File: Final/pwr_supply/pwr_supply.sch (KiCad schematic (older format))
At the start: 28 parts, among them IC1 AP64350SP-13, IC2 AP64350SP-13, T1 Transformer_1P_SS

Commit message: 
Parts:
- added C13, C14: 100n, Capacitor_SMD:C_1206_3216Metric_Pad1.33x1.80mm_HandSolder, symbol pspice:CAP
- C10, C9: footprint SamacSys_Parts:CAPC1608X90N -> Capacitor_SMD:C_1206_3216Metric_Pad1.33x1.80mm_HandSolder
- C11, C12: footprint SamacSys_Parts:CAPPRD225W50D680H1250 -> Capacitor_SMD:C_1206_3216Metric_Pad1.33x1.80mm_HandSolder
- C4, C8: footprint SamacSys_Parts:CAPC1005X56N -> Capacitor_SMD:C_1206_3216Metric_Pad1.33x1.80mm_HandSolder
- R5, R8: value 115k -> 309k
- RV1: footprint Varistor:RV_Disc_D15.5mm_W4.2mm_P7.5mm -> Varistor:RV_Disc_D16.5mm_W6.7mm_P7.5mm
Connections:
- wire segments 95 -> 98

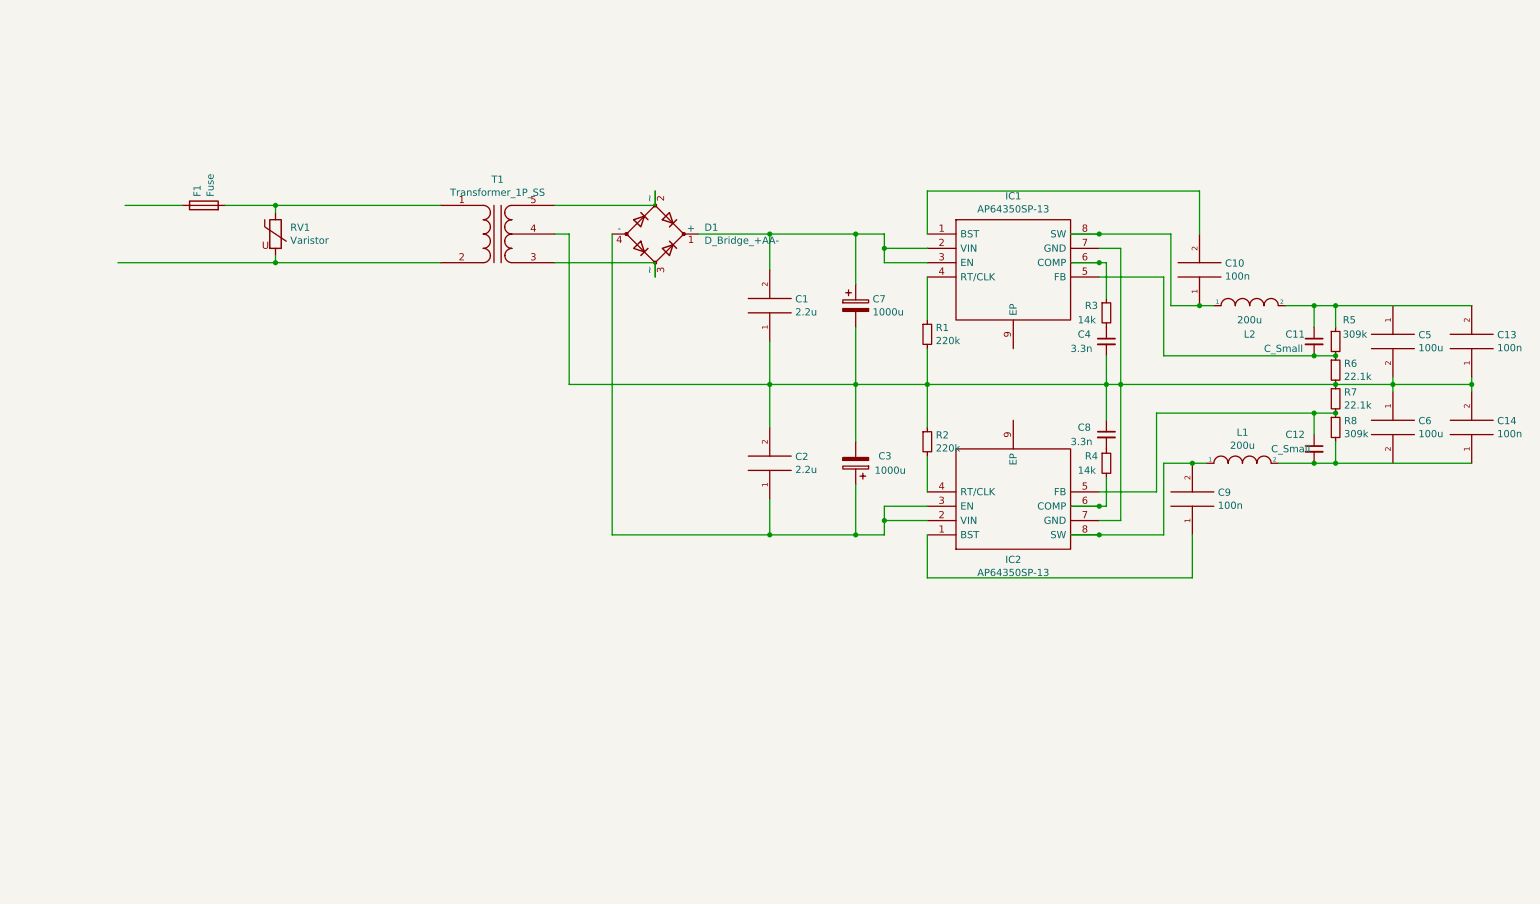
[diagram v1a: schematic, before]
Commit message: 
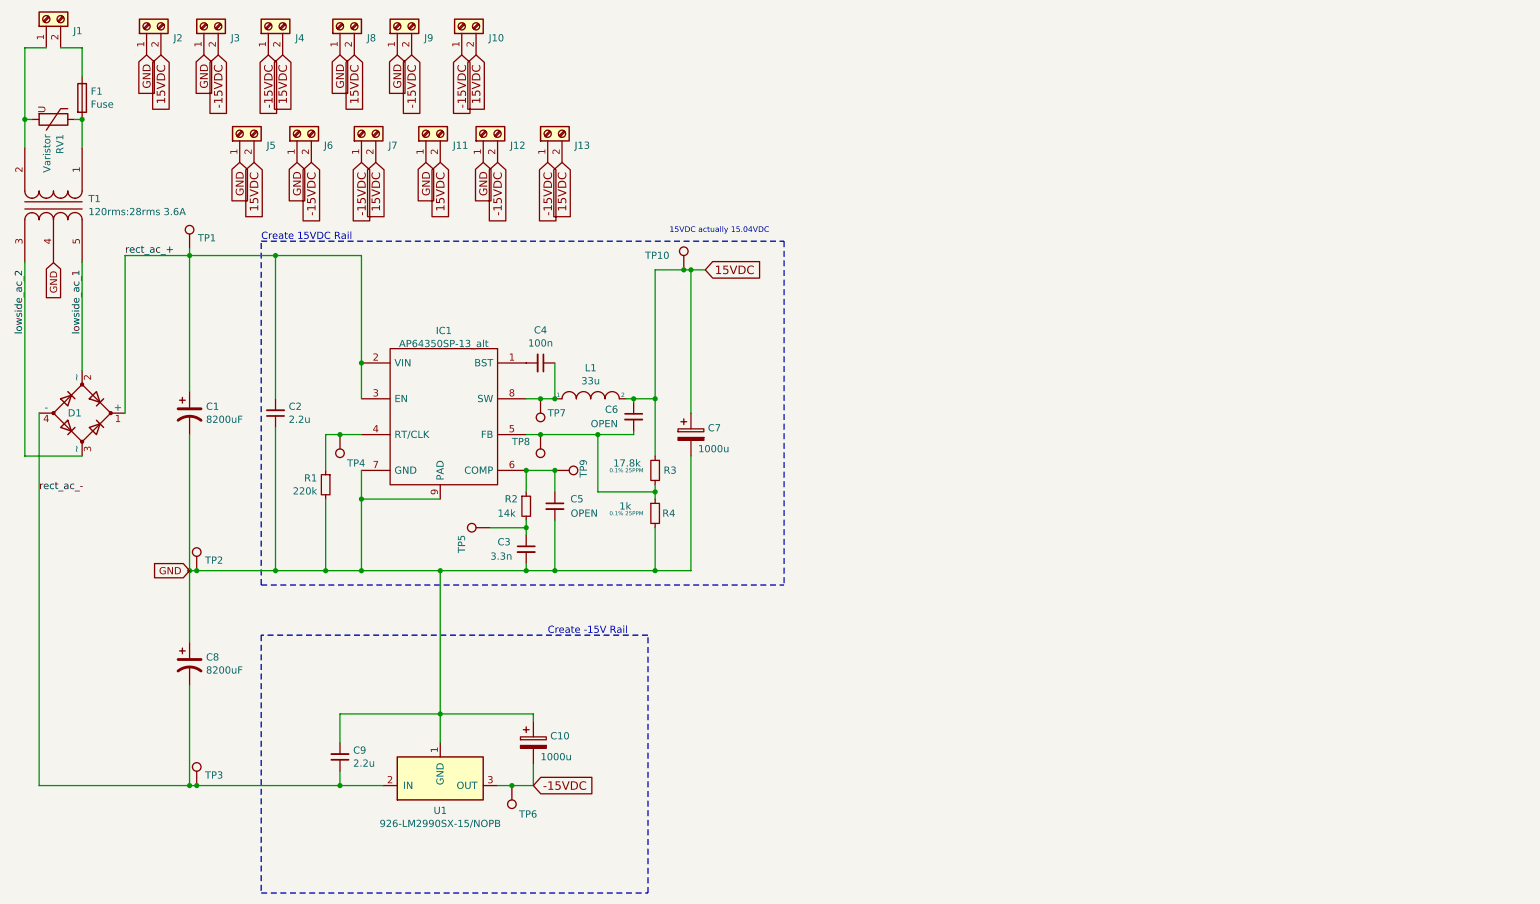
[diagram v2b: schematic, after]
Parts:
- removed C1, C2: 2.2u, Capacitor_SMD:C_1206_3216Metric_Pad1.33x1.80mm_HandSolder, symbol pspice:CAP
- removed C10, C13, C14, C9: 100n, Capacitor_SMD:C_1206_3216Metric_Pad1.33x1.80mm_HandSolder, symbol pspice:CAP
- removed C11, C12: C_Small, Capacitor_SMD:C_1206_3216Metric_Pad1.33x1.80mm_HandSolder, symbol Device:C_Small
- removed C3: 1000u, Capacitor_THT:CP_Radial_D16.0mm_P7.50mm, symbol Device:CP
- removed C5, C6: 100u, SamacSys_Parts:CAPPRD225W50D680H1250, symbol pspice:CAP
- removed C8: 3.3n, Capacitor_SMD:C_1206_3216Metric_Pad1.33x1.80mm_HandSolder, symbol Device:C_Small
- removed IC1, IC2: AP64350SP-13, SOIC127P600X163-9N, symbol SamacSys_Parts:AP64350SP-13
- removed L2: 200u, Inductor_THT:L_Axial_L9.5mm_D4.0mm_P2.54mm_Vertical_Fastron_SMCC, symbol pspice:INDUCTOR
- removed R5, R8: 309k, Resistor_SMD:R_1206_3216Metric_Pad1.30x1.75mm_HandSolder, symbol Device:R_Small
- removed R6, R7: 22.1k, Resistor_SMD:R_1206_3216Metric_Pad1.30x1.75mm_HandSolder, symbol Device:R_Small
- added C1, C8: 8200uF, Capacitor_THT:CP_Radial_D30.0mm_P10.00mm_SnapIn, symbol Device:CP1
- added C10: 1000u, Capacitor_THT:CP_Radial_D16.0mm_P7.50mm, symbol Device:CP
- added C2, C9: 2.2u, Capacitor_SMD:C_1210_3225Metric_Pad1.42x2.65mm_HandSolder, symbol Device:C_Small
- added C3: 3.3n, Capacitor_SMD:C_1210_3225Metric_Pad1.42x2.65mm_HandSolder, symbol Device:C_Small
- added C5, C6: OPEN, Capacitor_SMD:C_1210_3225Metric_Pad1.42x2.65mm_HandSolder, symbol Device:C_Small
- added IC1: AP64350SP-13_alt, SOIC127P600X163-9N, symbol SamacSys_Parts2:AP64350SP-13_alt
- added J1, J10, J11, J12, J13, J2, J3, J4, J5, J6, J7, J8, J9: Screw_Terminal_01x02, TerminalBlock:TerminalBlock_bornier-2_P5.08mm, symbol Connector:Screw_Terminal_01x02
- added TP1, TP10, TP2, TP3, TP4, TP5, TP6, TP7, TP8, TP9: TestPoint, Connector_PinHeader_2.54mm:PinHeader_1x01_P2.54mm_Vertical, symbol Connector:TestPoint
- added U1: 926-LM2990SX-15/NOPB, Package_TO_SOT_SMD:TO-263-3_TabPin2, symbol Regulator_Linear:LM2990SX-15
- C4: value 3.3n -> 100n; footprint Capacitor_SMD:C_1206_3216Metric_Pad1.33x1.80mm_HandSolder -> Capacitor_SMD:C_1210_3225Metric_Pad1.42x2.65mm_HandSolder
- D1: footprint SamacSys_Parts:TO385P410X1600X1290-4P -> Diode_THT:Diode_Bridge_19.0x3.5x10.0mm_P5.0mm
- L1: value 200u -> 33u; footprint Inductor_THT:L_Axial_L9.5mm_D4.0mm_P2.54mm_Vertical_Fastron_SMCC -> SamacSys_Parts:12RS333C
- R1: footprint Resistor_SMD:R_1206_3216Metric_Pad1.30x1.75mm_HandSolder -> Capacitor_SMD:C_1210_3225Metric_Pad1.42x2.65mm_HandSolder
- R2: value 220k -> 14k; footprint Resistor_SMD:R_1206_3216Metric_Pad1.30x1.75mm_HandSolder -> Capacitor_SMD:C_1210_3225Metric_Pad1.42x2.65mm_HandSolder
- R3: value 14k -> 17.8k; footprint Resistor_SMD:R_1206_3216Metric_Pad1.30x1.75mm_HandSolder -> Capacitor_SMD:C_1210_3225Metric_Pad1.42x2.65mm_HandSolder; Tolerance (none) -> 0.1% 25PPM
- R4: value 14k -> 1k; footprint Resistor_SMD:R_1206_3216Metric_Pad1.30x1.75mm_HandSolder -> Capacitor_SMD:C_1210_3225Metric_Pad1.42x2.65mm_HandSolder; Tolerance (none) -> 0.1% 25PPM
- T1: value Transformer_1P_SS -> 120rms:28rms 3.6A; footprint SamacSys_Parts:241-6-24 -> SamacSys_Parts:Transformer_Entry
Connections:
- net labels added: -15VDC, 15VDC, GND, lowside_ac_1, lowside_ac_2, rect_ac_+, rect_ac_-
- wire segments 98 -> 85
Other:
- note added: "15VDC actually 15.04VDC"
- note added: "Create -15V Rail"
- note added: "Create 15VDC Rail"
